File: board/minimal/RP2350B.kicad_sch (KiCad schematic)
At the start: 36 parts, among them SW1 SW_Bootsel, U1 W25Q128JVS, U11 RP2350B-QFN80, U2 AP63203WU, Y2 ABM8-272-T3

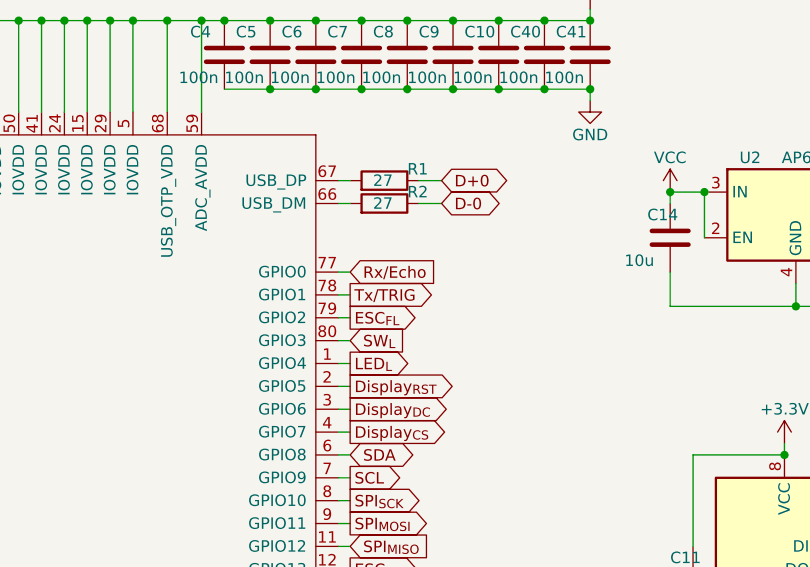
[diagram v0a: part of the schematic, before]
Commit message: add some connectors
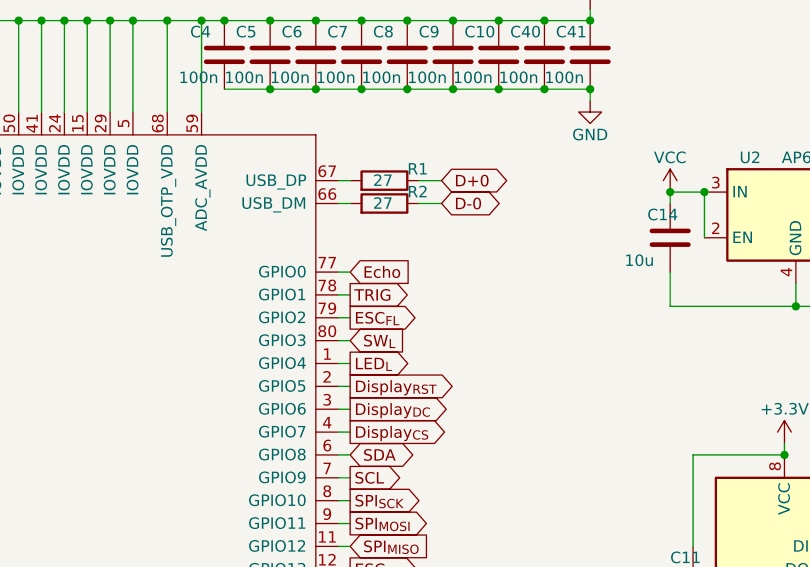
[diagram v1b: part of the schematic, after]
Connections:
- net Rx/Echo renamed Echo
- net Tx/TRIG renamed TRIG

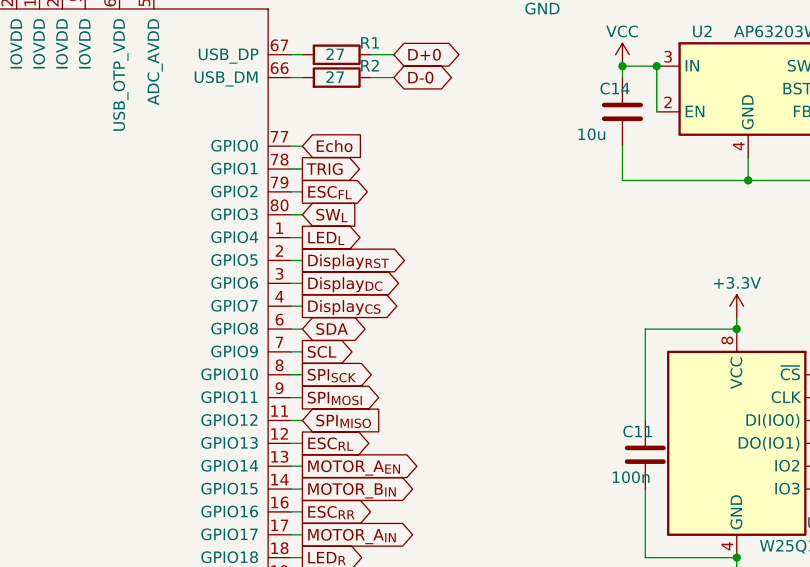
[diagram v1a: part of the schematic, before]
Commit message: change imu to BNO086
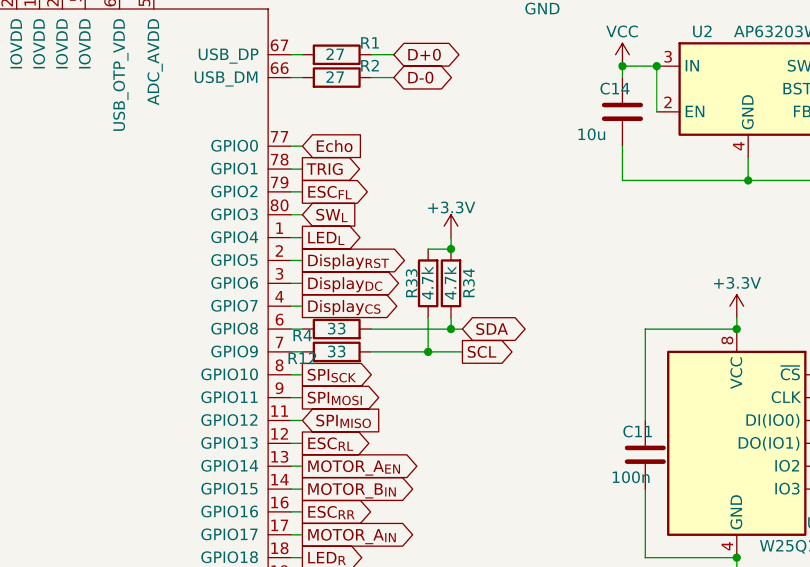
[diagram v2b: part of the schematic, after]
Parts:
- added R12, R4: 33, symbol Device:R
- added R33, R34: 4.7k, symbol Device:R
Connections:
- net +3.3V: now also R33.2, R34.2
- net SCL: now also R12.2, R33.1; no longer U11.7 (GPIO9)
- net SDA: now also R34.1, R4.2; no longer U11.6 (GPIO8)
- new net: R4.1, U11.6 (GPIO8)
- new net: R12.1, U11.7 (GPIO9)

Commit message: set footprint
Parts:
- C1: renamed from C42; footprint (none) -> Capacitor_SMD:C_0201_0603Metric
- C2: renamed from C43; footprint (none) -> Capacitor_SMD:C_0201_0603Metric
- C4: renamed from C44; footprint (none) -> Capacitor_SMD:C_0201_0603Metric
- L1: renamed from L2; footprint (none) -> AOTA-B201610S:L_pol_2016
- L2: renamed from L1; footprint Capacitor_SMD:C_0603_1608Metric -> AOTA-B201610S:L_pol_2016
- R1: renamed from R30; footprint (none) -> Resistor_SMD:R_0603_1608Metric
- R4: footprint (none) -> Resistor_SMD:R_0603_1608Metric
- R5: renamed from R12; footprint (none) -> Resistor_SMD:R_0603_1608Metric
- R8: renamed from R33; footprint (none) -> Resistor_SMD:R_0603_1608Metric
- R9: renamed from R34; footprint (none) -> Resistor_SMD:R_0603_1608Metric
- U1: renamed from U11; footprint (none) -> Package_DFN_QFN:QFN-80-1EP_10x10mm_P0.4mm_EP3.4x3.4mm_ThermalVias
- U2: renamed from U1; footprint Package_SO:SOIC-8_5.23x5.23mm_P1.27mm -> Package_SO:SOIC-8_5.3x5.3mm_P1.27mm
- Y1: renamed from Y2; footprint (none) -> ABRACON_Crystal:ABM8272T3
- renumbered C7 to C10, C8 to C11, C9 to C12, C10 to C13, C40 to C14, C41 to C15, C14 to C16, C11 to C17, C17 to C18, C18 to C19, C13 to C20, C15 to C21, C16 to C22, C1 to C3, C2 to C5, C3 to C6, C4 to C7, C5 to C8, C6 to C9, R3 to R10, R5 to R11, R1 to R2, R2 to R3, R31 to R6, R32 to R7, U2 to U3
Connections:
- net +3.3V: now also L2.1; no longer L2.2
- net at C20.2, U3.5 (SW): now also L2.2; no longer L2.1
- net Run: no longer names the net of U1.35 (RUN)
- no-connect marks 0 -> 1
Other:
- moved on the sheet: L2
